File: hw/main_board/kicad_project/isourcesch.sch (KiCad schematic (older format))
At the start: 0 parts

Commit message: refactored schematic, finalized gain/range
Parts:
- added C? (x8): 0.1uF, symbol C
- added C? (x7): 1uF, symbol C
- added C?: .1uF, symbol C
- added R?: 2K, symbol R
- added R?: 5K, symbol R
- added R?: 10K, symbol R
- added R?: 22K, symbol R
- added R?: 45K, symbol R
- added R?: 91K, symbol R
- added R?: 182K, symbol R
- added R?: 374K, symbol R
- added R?: 24K, symbol R
- added RV?: 1K, symbol POT
- added RV? (x2): 2K, symbol POT
- added RV? (x3): 5K, symbol POT
- added RV?: 10K, symbol POT
- added RV? (x2): 20K, symbol POT
- added U?: OP1177, symbol OP1177
- added U? (x2): AD5292, symbol AD5292
- added U?: AD8221, symbol AD8221
- added U? (x2): MAX338, symbol MAX338
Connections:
- new net: U?.2 (-), U?.6 (OUT), U?.6 (REF)
- new net: RV?.1, RV?.2, U?.4 (W), U?.5 (B)
- new net: RV?.3, U?.2 (Rg)
- new net: R?.2, U?.3 (A)
- new net: R?.1, U?.3 (Rg)
- new net: U?.7 (OUT), U?.8 (COM)
- new net: R?.1, U?.10 (OUT7)
- new net: R?.1, U?.11 (OUT6)
- new net: R?.1, U?.12 (OUT5)
- new net: R?.1, U?.4 (OUT1)
- new net: R?.1, U?.5 (OUT2)
- new net: R?.1, U?.6 (OUT3)
- new net: R?.1, U?.7 (OUT4)
- new net: R?.1, U?.9 (OUT8)
- new net: R?.2, RV?.1, RV?.2 (x8)
- new net: C?.1, U?.7 (EXT_CAP)
- new net AGND: C?.2, C?.2, C?.2, C?.2, C?.2, C?.2, C?.2, C?.2, C?.2, C?.2, C?.2, C?.2, C?.2, C?.2, C?.2, C?.2, U?.14 (GND), U?.9 (GND)
- new net AVDD: C?.1, C?.1, C?.1, C?.1, U?.13 (V+), U?.6 (VDD)
- new net AVDD_3V3: C?.1, U?.8 (Vlogic)
- new net AVSS: C?.1, C?.1, C?.1, C?.1, U?.2 (VSS), U?.3 (V-)
- new net GAIN_BUS0: U?.1 (RESET)
- new net GAIN_BUS1: U?.10 (DIN)
- new net GAIN_BUS2: U?.11 (SCLK)
- new net GAIN_BUS3: U?.12 (SYNC)
- new net GAIN_BUS4: U?.14 (RDY)
- new net IOUT: RV?.3, RV?.3, U?.3 (+)
- new net RANGE_MUX0: U?.2 (EN)
- new net RANGE_MUX1: U?.1 (A0)
- new net RANGE_MUX2: U?.16 (A1)
- new net RANGE_MUX3: U?.15 (A2)
- new net VDD: C?.1, C?.1, U?.7 (V+), U?.8 (V+)
- new net VSS: C?.1, C?.1, U?.4 (V-), U?.5 (V-)
- new net Vin+: U?.4 (+)
- new net Vin-: U?.1 (-)

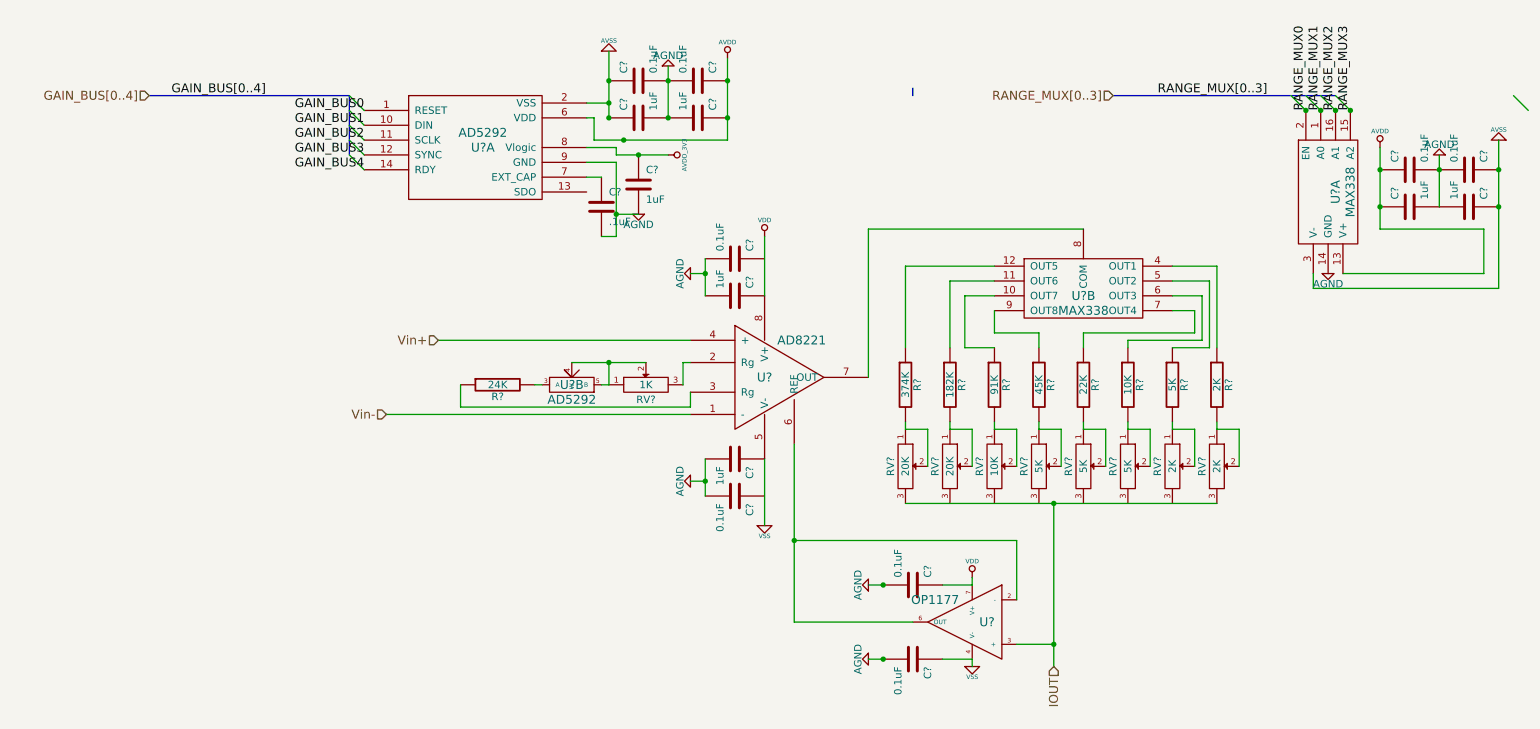
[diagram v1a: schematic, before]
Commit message: started mainboard pcb layout, fixing small things in schematic, TODO: schematic connector symbols and pads
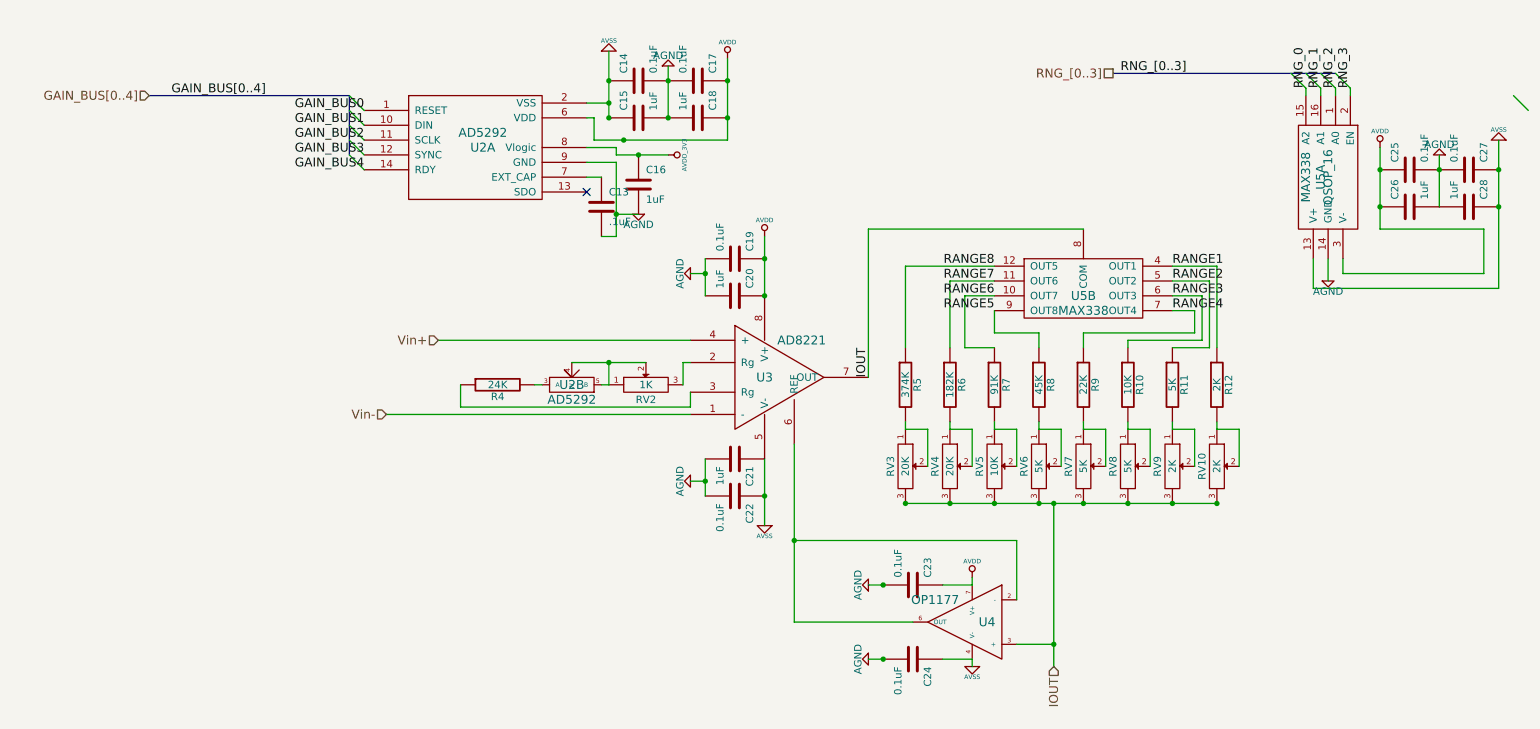
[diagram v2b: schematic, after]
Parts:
- removed U?: MAX338, symbol MAX338
- added unit 1 of U5
- C13, C14, C15, C16, C17, C18, C19, C20, C21, C22, C23, C24, C25, C26, C27, C28: renamed from C?; footprint (none) -> 0603
- R10, R11, R12, R4, R5, R6, R7, R8, R9: renamed from R?; footprint (none) -> 0603
- RV10, RV2, RV3, RV4, RV5, RV6, RV7, RV8, RV9: renamed from RV?; footprint (none) -> 3224X
- U2: renamed from U?; footprint (none) -> MSOP-10
- U3: renamed from U?; footprint (none) -> TSSOP_14
- U4: renamed from U?; footprint (none) -> MSOP_8
- U5: renamed from U?; footprint (none) -> QSOP_16
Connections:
- net VDD is gone; now on net AVDD: C20.1, C23.1, U3.8 (V+), U4.7 (V+)
- net VSS is gone; now on net AVSS: C21.1, C24.1, U3.5 (V-), U4.4 (V-)
- net AGND: now also U5.14 (GND)
- net AVDD: now also C19.1, U5.3 (V-)
- net AVSS: now also C22.1, U5.13 (V+)
- net IOUT: now also RV4.3, RV5.3, RV6.3, RV7.3, RV8.3, RV9.3, U3.7 (OUT), U5.8 (COM)
- net RANGE6: now reaches R7.1, U5.10 (OUT7)
- net RANGE7: now reaches R6.1, U5.11 (OUT6)
- net RANGE8: now reaches R5.1, U5.12 (OUT5)
- net RANGE1: now reaches R12.1, U5.4 (OUT1)
- net RANGE2: now reaches R11.1, U5.5 (OUT2)
- net RANGE3: now reaches R10.1, U5.6 (OUT3)
- net RANGE4: now reaches R9.1, U5.7 (OUT4)
- net RANGE5: now reaches R8.1, U5.9 (OUT8)
- new net RNG_0: U5.15 (A2)
- new net RNG_1: U5.16 (A1)
- new net RNG_2: U5.1 (A0)
- new net RNG_3: U5.2 (EN)
- no-connect marks 0 -> 1

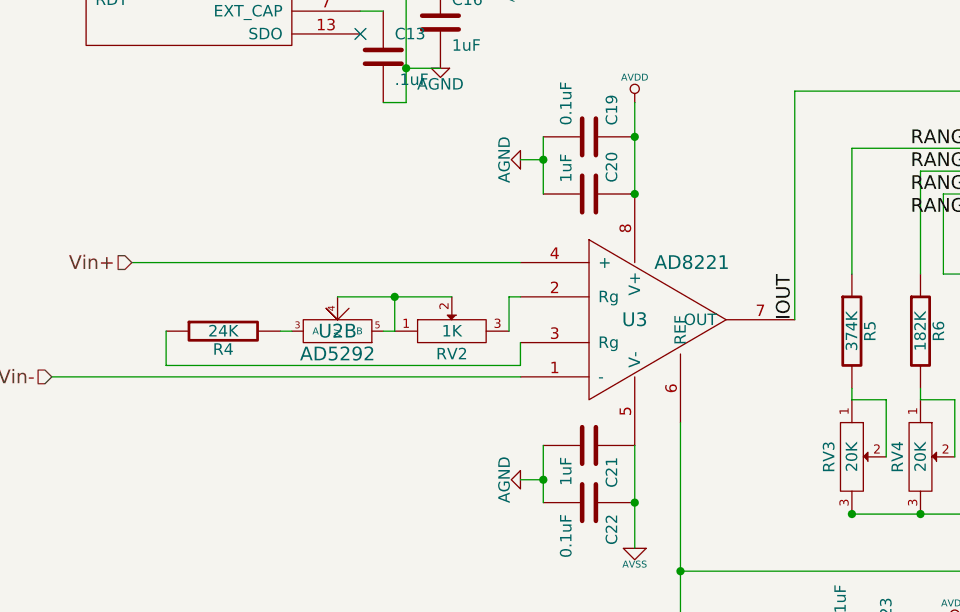
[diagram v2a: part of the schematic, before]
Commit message: final rework of mux board, finalizing stacking connectors, almost there
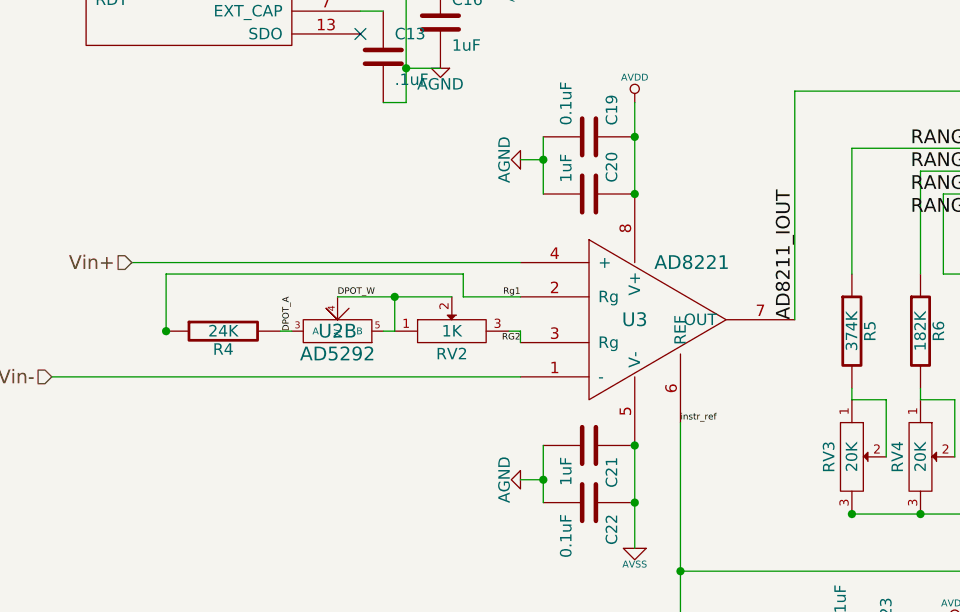
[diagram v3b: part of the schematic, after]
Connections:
- net IOUT: no longer U3.7 (OUT), U5.8 (COM)
- net instr_ref: now reaches U3.6 (REF), U4.2 (-), U4.6 (OUT)
- net DPOT_W: now reaches RV2.1, RV2.2, U2.4 (W), U2.5 (B)
- net RG2: now reaches RV2.3
- net RG2: now also U3.3 (Rg); no longer U3.2 (Rg)
- net DPOT_A: now reaches R4.2, U2.3 (A)
- net Rg1: now reaches R4.1
- net Rg1: now also U3.2 (Rg); no longer U3.3 (Rg)
- new net AD8211_IOUT: U3.7 (OUT), U5.8 (COM)
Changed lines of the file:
@@
 EESchema Schematic File Version 2
-LIBS:power
-LIBS:device
-LIBS:transistors
-LIBS:conn
-LIBS:linear
-LIBS:regul
-LIBS:74xx
-LIBS:cmos4000
-LIBS:adc-dac
-LIBS:memory
-LIBS:xilinx
-LIBS:special
-LIBS:microcontrollers
-LIBS:dsp
-LIBS:microchip
-LIBS:analog_switches
-LIBS:motorola
-LIBS:texas
-LIBS:intel
-LIBS:audio
-LIBS:interface
-LIBS:digital-audio
-LIBS:philips
-LIBS:display
-LIBS:cypress
-LIBS:siliconi
-LIBS:opto
-LIBS:atmel
-LIBS:contrib
-LIBS:valves
 LIBS:ddslib
-LIBS:demuxcomplib
-LIBS:tdsc-kicad-convert
 LIBS:tDCS_driver-cache
 EELAYER 24 0
@@
 $EndComp
 $Comp
-L AGND #PWR030
+L AGND #PWR036
 U 1 1 531691D2
 P 6050 4900
-F 0 "#PWR030" H 6050 4900 40  0001 C CNN
+F 0 "#PWR036" H 6050 4900 40  0001 C CNN
 F 1 "AGND" H 6050 4830 50  0000 C CNN
 F 2 "" H 6050 4900 60  0001 C CNN
@@
 $EndComp
 $Comp
-L AGND #PWR031
+L AGND #PWR037
 U 1 1 531691DE
 P 6050 4400
-F 0 "#PWR031" H 6050 4400 40  0001 C CNN
+F 0 "#PWR037" H 6050 4400 40  0001 C CNN
 F 1 "AGND" H 6050 4330 50  0000 C CNN
 F 2 "" H 6050 4400 60  0001 C CNN
@@
 $EndComp
 $Comp
-L AGND #PWR032
+L AGND #PWR038
 U 1 1 53169208
 P 4850 2300
-F 0 "#PWR032" H 4850 2300 40  0001 C CNN
+F 0 "#PWR038" H 4850 2300 40  0001 C CNN
 F 1 "AGND" H 4850 2230 50  0000 C CNN
 F 2 "" H 4850 2300 60  0001 C CNN
@@
 $EndComp
 $Comp
-L AGND #PWR033
+L AGND #PWR039
 U 1 1 5316920E
 P 4850 3700
-F 0 "#PWR033" H 4850 3700 40  0001 C CNN
+F 0 "#PWR039" H 4850 3700 40  0001 C CNN
 F 1 "AGND" H 4850 3630 50  0000 C CNN
 F 2 "" H 4850 3700 60  0001 C CNN
@@
 $EndComp
 $Comp
-L AGND #PWR034
+L AGND #PWR040
 U 1 1 5316DC90
 P 9900 1500
-F 0 "#PWR034" H 9900 1500 40  0001 C CNN
+F 0 "#PWR040" H 9900 1500 40  0001 C CNN
 F 1 "AGND" H 9900 1430 50  0000 C CNN
 F 2 "" H 9900 1500 60  0001 C CNN
@@
 $EndComp
 $Comp
-L AVDD #PWR035
+L AVDD #PWR041
 U 1 1 5316DC96
 P 9500 1450
-F 0 "#PWR035" H 9500 1550 30  0001 C CNN
+F 0 "#PWR041" H 9500 1550 30  0001 C CNN
 F 1 "AVDD" H 9500 1560 30  0000 C CNN
 F 2 "" H 9500 1450 60  0001 C CNN
@@
 $EndComp
 $Comp
-L AVSS #PWR036
+L AVSS #PWR042
 U 1 1 5316DCAA
 P 10300 1400
-F 0 "#PWR036" H 10300 1400 30  0001 C CNN
+F 0 "#PWR042" H 10300 1400 30  0001 C CNN
 F 1 "AVSS" H 10300 1330 30  0000 C CNN
 F 2 "" H 10300 1400 60  0001 C CNN
@@
 $EndComp
 $Comp
-L AGND #PWR037
+L AGND #PWR043
 U 1 1 5316DCB0
 P 9150 2350
-F 0 "#PWR037" H 9150 2350 40  0001 C CNN
+F 0 "#PWR043" H 9150 2350 40  0001 C CNN
 F 1 "AGND" H 9150 2280 50  0000 C CNN
 F 2 "" H 9150 2350 60  0001 C CNN
@@
 RNG_[0..3]
 $Comp
-L AVDD_3V3 #PWR038
+L AVDD_3V3 #PWR044
 U 1 1 5316EBB1
 P 4700 1500
-F 0 "#PWR038" H 4700 1600 30  0001 C CNN
+F 0 "#PWR044" H 4700 1600 30  0001 C CNN
 F 1 "AVDD_3V3" H 4700 1610 30  0000 C CNN
 F 2 "" H 4700 1500 60  0001 C CNN
@@
 $EndComp
 $Comp
-L AGND #PWR039
+L AGND #PWR045
 U 1 1 5316EBC3
 P 4500 1900
-F 0 "#PWR039" H 4500 1900 40  0001 C CNN
+F 0 "#PWR045" H 4500 1900 40  0001 C CNN
 F 1 "AGND" H 4500 1830 50  0000 C CNN
 F 2 "" H 4500 1900 60  0001 C CNN
@@
 $EndComp
 $Comp
-L AVSS #PWR040
+L AVSS #PWR046
 U 1 1 5316EBC9
 P 4300 800
-F 0 "#PWR040" H 4300 800 30  0001 C CNN
+F 0 "#PWR046" H 4300 800 30  0001 C CNN
 F 1 "AVSS" H 4300 730 30  0000 C CNN
 F 2 "" H 4300 800 60  0001 C CNN
@@
 $EndComp
 $Comp
-L AVDD #PWR041
+L AVDD #PWR047
 U 1 1 5316EBDB
 P 5100 850
-F 0 "#PWR041" H 5100 950 30  0001 C CNN
+F 0 "#PWR047" H 5100 950 30  0001 C CNN
 F 1 "AVDD" H 5100 960 30  0000 C CNN
 F 2 "" H 5100 850 60  0001 C CNN
@@
 $EndComp
 $Comp
-L AGND #PWR042
+L AGND #PWR048
 U 1 1 5316EBE1
 P 4700 900
-F 0 "#PWR042" H 4700 900 40  0001 C CNN
+F 0 "#PWR048" H 4700 900 40  0001 C CNN
 F 1 "AGND" H 4700 830 50  0000 C CNN
 F 2 "" H 4700 900 60  0001 C CNN
@@
 GAIN_BUS[0..4]
 $Comp
-L AVDD #PWR043
+L AVDD #PWR049
 U 1 1 531828B9
 P 5350 2050
-F 0 "#PWR043" H 5350 2150 30  0001 C CNN
+F 0 "#PWR049" H 5350 2150 30  0001 C CNN
 F 1 "AVDD" H 5350 2160 30  0000 C CNN
 F 2 "" H 5350 2050 60  0001 C CNN
@@
 $EndComp
 $Comp
-L AVSS #PWR044
+L AVSS #PWR050
 U 1 1 531828C9
 P 5350 4000
-F 0 "#PWR044" H 5350 4000 30  0001 C CNN
+F 0 "#PWR050" H 5350 4000 30  0001 C CNN
 F 1 "AVSS" H 5350 3930 30  0000 C CNN
 F 2 "" H 5350 4000 60  0001 C CNN
@@
 $EndComp
 $Comp
-L AVSS #PWR045
+L AVSS #PWR051
 U 1 1 531828D9
 P 6750 4950
-F 0 "#PWR045" H 6750 4950 30  0001 C CNN
+F 0 "#PWR051" H 6750 4950 30  0001 C CNN
 F 1 "AVSS" H 6750 4880 30  0000 C CNN
 F 2 "" H 6750 4950 60  0001 C CNN
@@
 $EndComp
 $Comp
-L AVDD #PWR046
+L AVDD #PWR052
 U 1 1 531828E9
 P 6750 4350
-F 0 "#PWR046" H 6750 4450 30  0001 C CNN
+F 0 "#PWR052" H 6750 4450 30  0001 C CNN
 F 1 "AVDD" H 6750 4460 30  0000 C CNN
 F 2 "" H 6750 4350 60  0001 C CNN
@@
 Wire Wire Line
 	4950 2300 4850 2300
-Wire Wire Line
-	3300 3200 4850 3200
-Wire Wire Line
-	4850 3200 4850 3100
 Connection ~ 6150 4400
 Wire Wire Line
@@
 Connection ~ 5550 4100
 Wire Wire Line
-	3300 3050 3300 3200
-Wire Wire Line
 	3800 3050 3850 3050
-Wire Wire Line
-	4800 2900 4800 3050
 Wire Wire Line
 	4300 3050 4250 3050
@@
 Connection ~ 4300 2900
 Wire Wire Line
-	4850 2900 4800 2900
+	4600 2900 4850 2900
 Wire Wire Line
 	4050 2900 4550 2900
@@
 RANGE8
 Text Label 6050 3000 1    60   ~ 0
-IOUT
+AD8211_IOUT
+Text Label 4850 2900 2    28   ~ 0
+Rg1
+Text Label 4850 3100 2    28   ~ 0
+RG2
+Text Label 3850 3050 1    28   ~ 0
+DPOT_A
+Text Label 4050 2900 0    28   ~ 0
+DPOT_W
+Text Label 5550 3450 0    28   ~ 0
+instr_ref
+Connection ~ 5350 3550
+Wire Wire Line
+	4600 2900 4600 2800
+Wire Wire Line
+	4600 2800 3300 2800
+Connection ~ 3300 3050
+Wire Wire Line
+	4850 3100 4850 3050
+Wire Wire Line
+	4850 3050 4800 3050
+Wire Wire Line
+	3300 2800 3300 3050
 $EndSCHEMATC

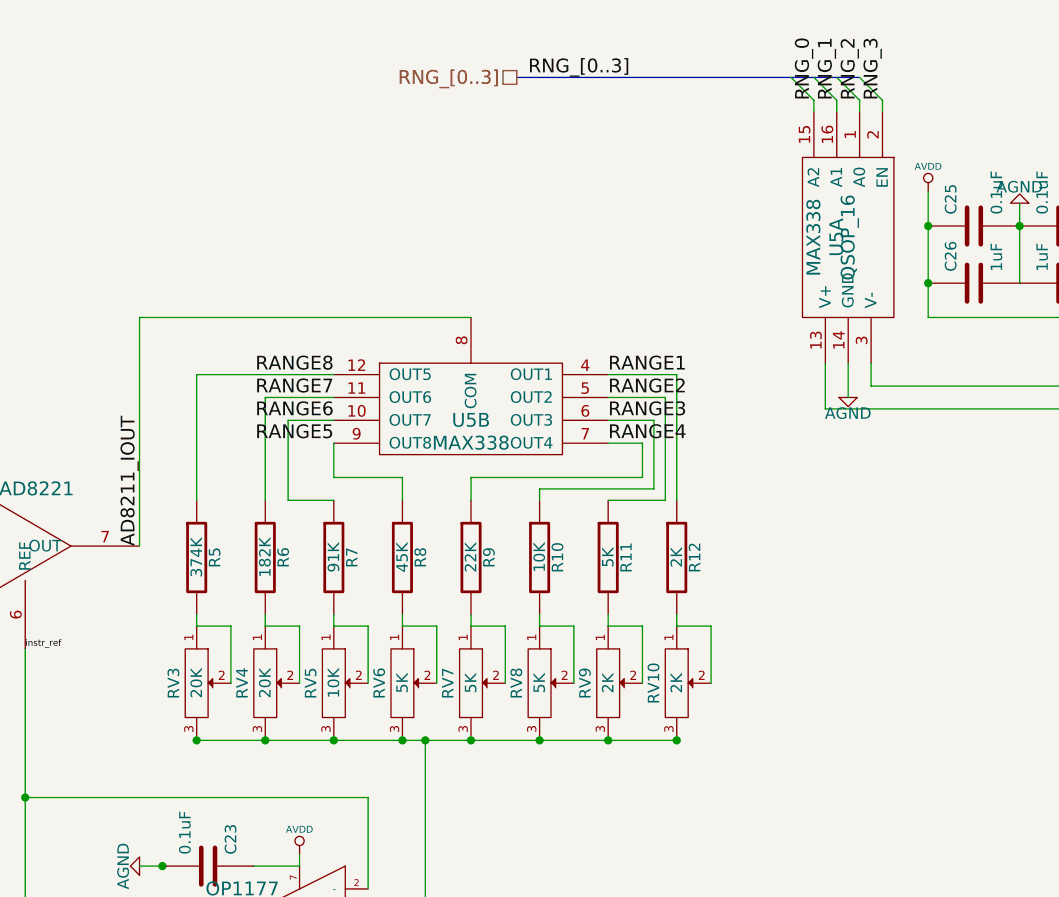
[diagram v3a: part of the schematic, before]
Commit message: finished component layout on mainboard, need to route power planes and the digital control signal lines
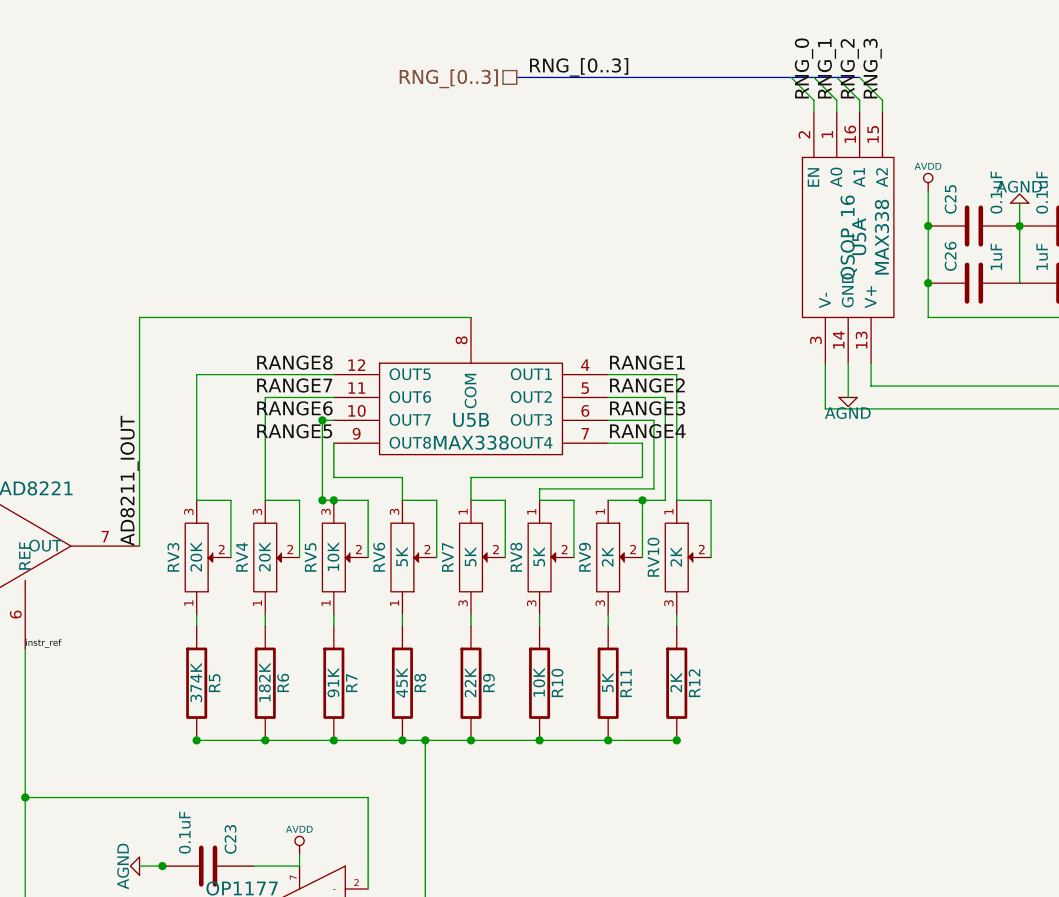
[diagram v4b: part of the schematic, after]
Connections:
- net AVDD: now also U5.13 (V+); no longer U5.3 (V-)
- net AVSS: now also U5.3 (V-); no longer U5.13 (V+)
- net IOUT: now also R10.2, R11.2, R12.2, R5.2, R6.2, R7.2, R8.2, R9.2; no longer RV10.3, RV3.3, RV4.3, RV5.3, RV6.3, RV7.3, RV8.3, RV9.3
- net RANGE1: now also RV10.1, RV10.2; no longer R12.1
- net RANGE2: now also RV9.1, RV9.2; no longer R11.1
- net RANGE3: now also RV8.1, RV8.2; no longer R10.1
- net RANGE4: now also RV7.1, RV7.2; no longer R9.1
- net RANGE5: now also RV6.2, RV6.3; no longer R8.1
- net RANGE6: now also RV5.2, RV5.3; no longer R7.1
- net RANGE7: now also RV4.2, RV4.3; no longer R6.1
- net RANGE8: now also RV3.2, RV3.3; no longer R5.1
- net RNG_0: now also U5.2 (EN); no longer U5.15 (A2)
- net RNG_1: now also U5.1 (A0); no longer U5.16 (A1)
- net RNG_2: now also U5.16 (A1); no longer U5.1 (A0)
- net RNG_3: now also U5.15 (A2); no longer U5.2 (EN)
- new net: R12.1, RV10.3
- new net: R11.1, RV9.3
- new net: R10.1, RV8.3
- new net: R9.1, RV7.3
- new net: R8.1, RV6.1
- new net: R7.1, RV5.1
- new net: R6.1, RV4.1
- new net: R5.1, RV3.1
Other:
- moved on the sheet: R10, R11, R12, R5, R6, R7, R8, R9, RV10, RV3, RV4, RV5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
